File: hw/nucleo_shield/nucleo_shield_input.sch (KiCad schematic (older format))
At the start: 22 parts, among them P1 CONN_INH1, P5 CONN_INH2, U3 LTV-847, U4 LTV-847, U5 LTV-847, U6 LTV-847

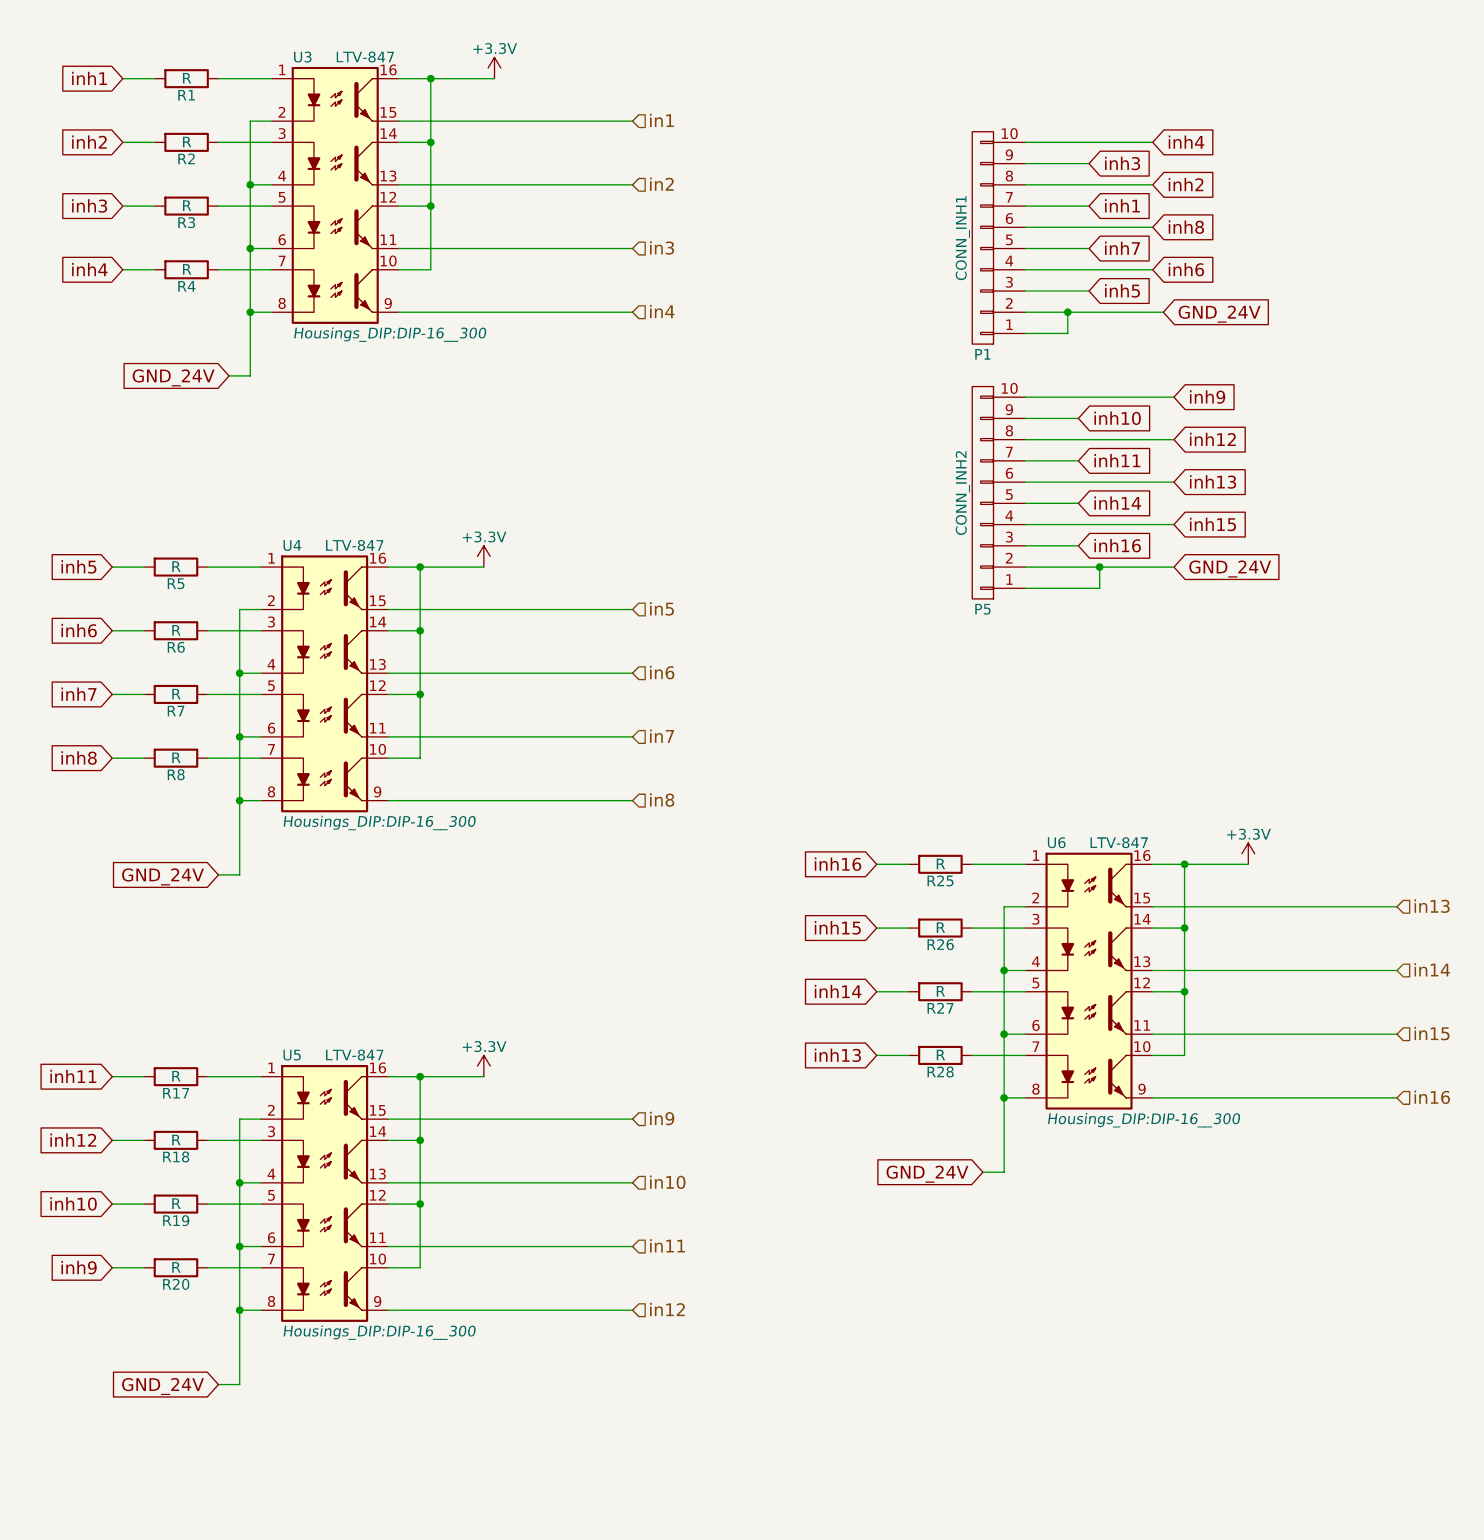
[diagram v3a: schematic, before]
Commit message: Nucleo: add RS485 headers, add CMS pulldown  resistors
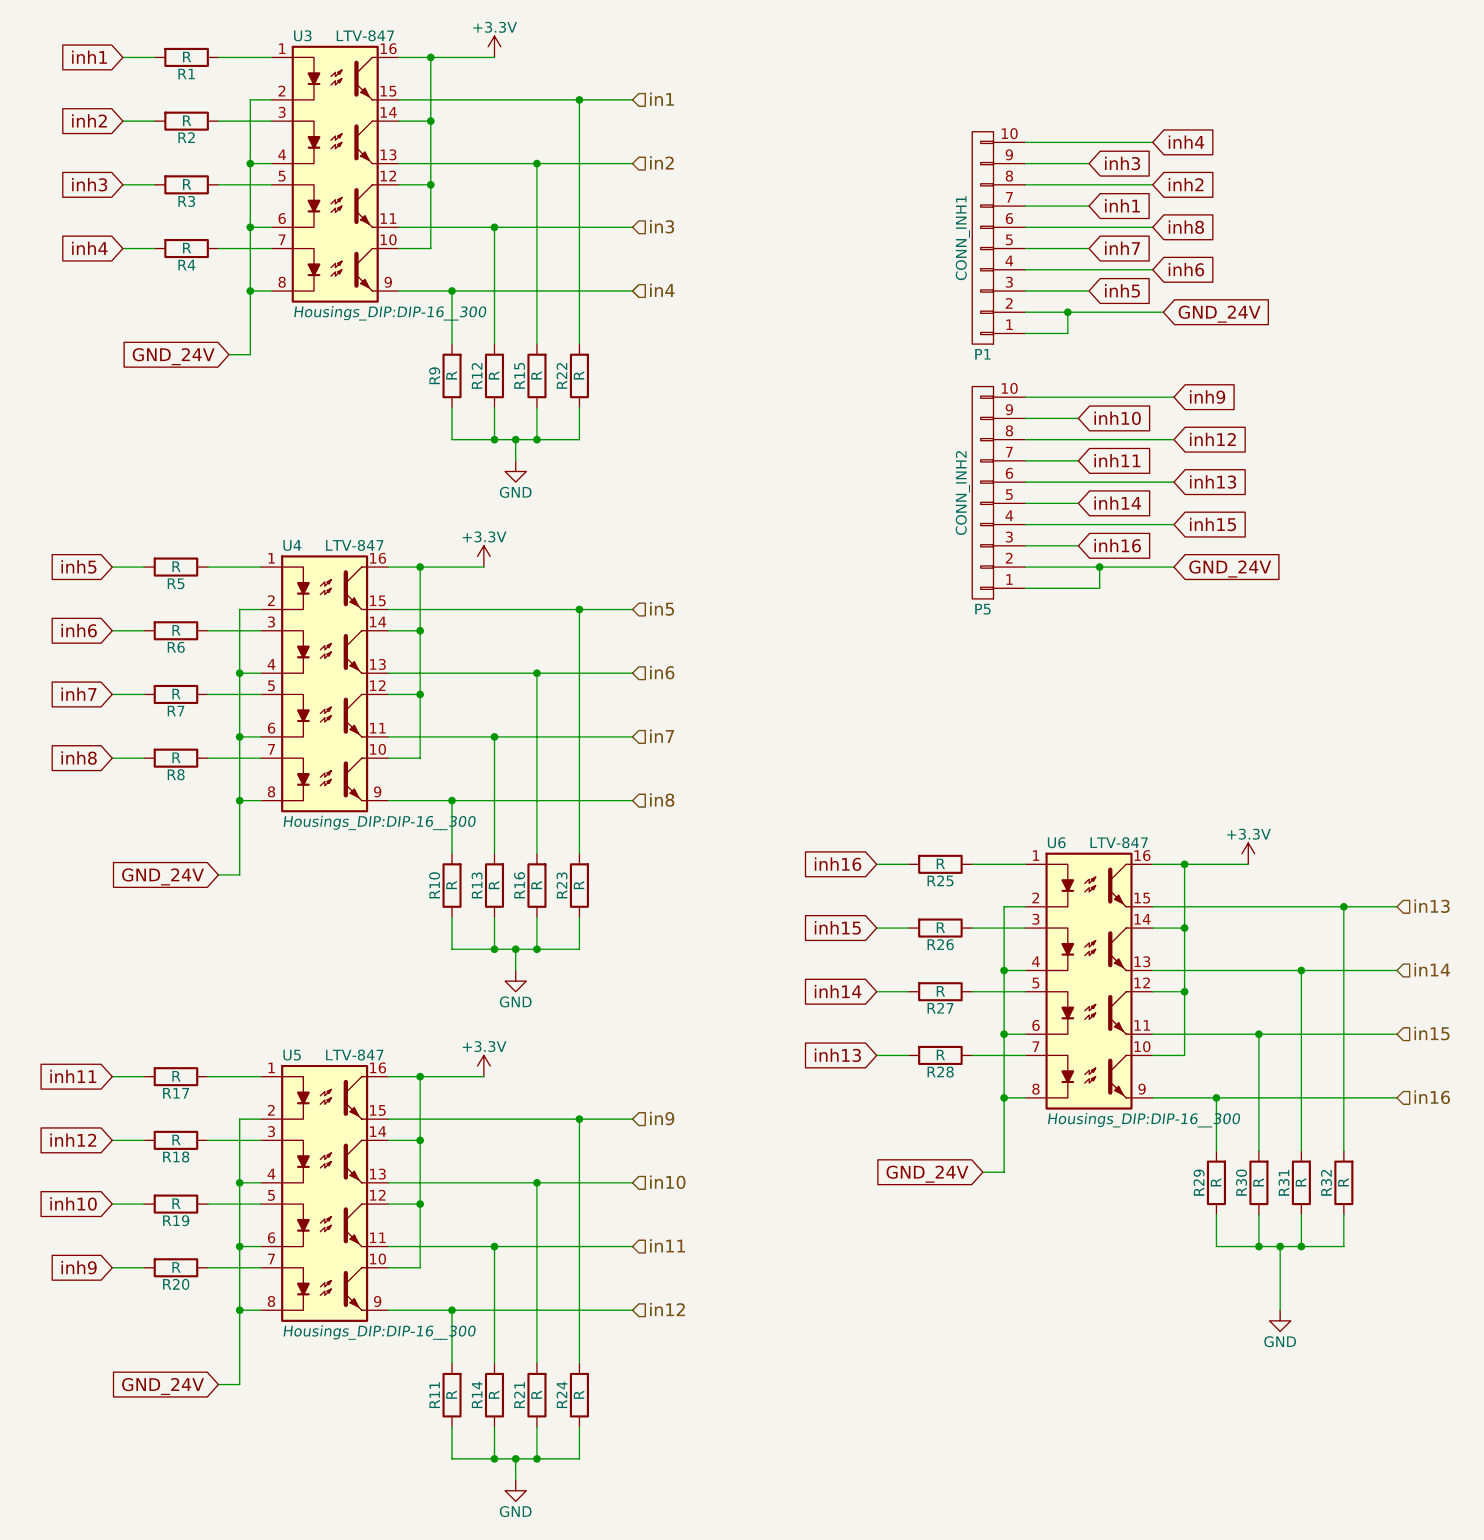
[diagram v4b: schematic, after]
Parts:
- added R10, R11, R12, R13, R14, R15, R16, R21, R22, R23, R24, R29, R30, R31, R32, R9: R, Resistors_SMD:R_0805_HandSoldering, symbol R
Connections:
- net in1: now also R22.2
- net in10: now also R21.2
- net in11: now also R14.2
- net in12: now also R11.2
- net in13: now also R32.2
- net in14: now also R31.2
- net in15: now also R30.2
- net in16: now also R29.2
- net in2: now also R15.2
- net in3: now also R12.2
- net in4: now also R9.2
- net in5: now also R23.2
- net in6: now also R16.2
- net in7: now also R13.2
- net in8: now also R10.2
- net in9: now also R24.2
- new net GND: R10.1, R11.1, R12.1, R13.1, R14.1, R15.1, R16.1, R21.1, R22.1, R23.1, R24.1, R29.1, R30.1, R31.1, R32.1, R9.1
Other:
- moved on the sheet: R1, R2, R3, R4, U3
